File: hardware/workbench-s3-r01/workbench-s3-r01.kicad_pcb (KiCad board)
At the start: 2 copper layers, 126 x 135 mm, 52 parts, among them J1 YD P1 / RIGHT SOCKET / 1x22, J2 DISPLAY HARNESS / 3V3, J4 EXPANSION / 3V3 IO, J5 EXTERNAL BOOT / GPIO0 TO GND, J6 EXTERNAL RESET / EN TO GND, J7 YD P2 / LEFT SOCKET / 1x22, SW1 KEY_1 MX HOTSWAP, SW10 KEY_10 MX HOTSWAP, SW11 KEY_11 MX HOTSWAP, SW12 KEY_12 MX HOTSWAP, SW13 KEY_13 MX HOTSWAP, SW14 KEY_14 MX HOTSWAP, SW15 KEY_15 MX HOTSWAP, SW16 KEY_16 MX HOTSWAP, SW17 KEY_17 MX HOTSWAP, SW18 KEY_18 MX HOTSWAP, SW2 KEY_2 MX HOTSWAP, SW3 KEY_3 MX HOTSWAP, SW4 KEY_4 MX HOTSWAP, SW5 KEY_5 MX HOTSWAP, SW6 KEY_6 MX HOTSWAP, SW7 KEY_7 MX HOTSWAP, SW8 KEY_8 MX HOTSWAP, SW9 KEY_9 MX HOTSWAP

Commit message: Update application workflows and supporting components
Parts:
- removed H1, H2, H3, H4, H5: M3 head <=5.6mm, MountingHole_M3_5.6mm_Head
- added H_L1: M3 head <=5.6mm, MountingHole_M3_5.6mm_Head, F.Cu at (172.0, 233.0)
- added H_L2: M3 head <=5.6mm, MountingHole_M3_5.6mm_Head, F.Cu at (54.0, 233.0)
- added H_L3: M3 head <=5.6mm, MountingHole_M3_5.6mm_Head, F.Cu at (172.0, 155.0)
- added H_L4: M3 head <=5.6mm, MountingHole_M3_5.6mm_Head, F.Cu at (54.0, 155.0)
- added H_U1: M3 head <=5.6mm, MountingHole_M3_5.6mm_Head, F.Cu at (54.0, 54.0)
- added H_U2: M3 head <=5.6mm, MountingHole_M3_5.6mm_Head, F.Cu at (172.0, 54.0)
- added H_U3: M3 head <=5.6mm, MountingHole_M3_5.6mm_Head, F.Cu at (54.0, 144.0)
- added H_U4: M3 head <=5.6mm, MountingHole_M3_5.6mm_Head, F.Cu at (172.0, 144.0)
- added J8: LOWER / IDC20 TO J9 / 1:1, IDC-Header_2x10_P2.54mm_Vertical, F.Cu at (129.0, 212.0)
- added J9: UPPER / IDC20 TO J8 / 1:1, IDC-Header_2x10_P2.54mm_Vertical, B.Cu at (162.0, 65.0)
- added MB1: MouseBites_6x0.5_P0.8, MouseBites_6x0.5_P0.8, F.Cu at (70.0, 148.8)
- added MB2: MouseBites_6x0.5_P0.8, MouseBites_6x0.5_P0.8, F.Cu at (70.0, 150.2)
- added MB3: MouseBites_6x0.5_P0.8, MouseBites_6x0.5_P0.8, F.Cu at (113.0, 148.8)
- added MB4: MouseBites_6x0.5_P0.8, MouseBites_6x0.5_P0.8, F.Cu at (113.0, 150.2)
- added MB5: MouseBites_6x0.5_P0.8, MouseBites_6x0.5_P0.8, F.Cu at (156.0, 148.8)
- added MB6: MouseBites_6x0.5_P0.8, MouseBites_6x0.5_P0.8, F.Cu at (156.0, 150.2)
- moved J4 209.8 mm to (166.0, 234.0), turned to -90 degrees
- moved J6 180.3 mm to (102.0, 233.0), turned to -90 degrees
- moved J5 179.0 mm to (111.0, 233.0), turned to -90 degrees
- moved R3 164.0 mm to (104.0, 225.0), turned to 180 degrees
- moved J1 123.9 mm to (64.3, 181.8), turned to 0 degrees
- moved J7 89.6 mm to (89.7, 181.8), turned to 0 degrees
- moved D10 38.4 mm to (124.0, 111.0)
- moved D11 38.4 mm to (143.1, 111.0)
- moved D12 38.4 mm to (162.1, 111.0)
- moved D7 38.4 mm to (66.9, 111.0)
- moved D8 38.4 mm to (85.9, 111.0)
- moved D9 38.4 mm to (105.0, 111.0)
- moved SW10 38.4 mm to (124.0, 117.0)
- moved SW11 38.4 mm to (143.1, 117.0)
- moved SW12 38.4 mm to (162.1, 117.0)
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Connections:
- net /KEY_10_A renamed /UP_KEY_10_A
- net /KEY_11_A renamed /UP_KEY_11_A
- net /KEY_12_A renamed /UP_KEY_12_A
- net /KEY_13_A renamed /UP_KEY_13_A
- net /KEY_14_A renamed /UP_KEY_14_A
- net /KEY_15_A renamed /UP_KEY_15_A
- net /KEY_16_A renamed /UP_KEY_16_A
- net /KEY_17_A renamed /UP_KEY_17_A
- net /KEY_18_A renamed /UP_KEY_18_A
- net /KEY_1_A renamed /UP_KEY_1_A
- net /KEY_2_A renamed /UP_KEY_2_A
- net /KEY_3_A renamed /UP_KEY_3_A
- net /KEY_4_A renamed /UP_KEY_4_A
- net /KEY_5_A renamed /UP_KEY_5_A
- net /KEY_6_A renamed /UP_KEY_6_A
- net /KEY_7_A renamed /UP_KEY_7_A
- net /KEY_8_A renamed /UP_KEY_8_A
- net /KEY_9_A renamed /UP_KEY_9_A
- C1 pad 1: /+3V3 -> /UP_3V3
- C1 pad 2: /GND -> /UP_GND
- C2 pad 1: /+3V3 -> /UP_3V3
- C2 pad 2: /GND -> /UP_GND
- D1 pad 1: /GPIO4 -> /UP_GPIO4
- D10 pad 1: /GPIO5 -> /UP_GPIO5
- D11 pad 1: /GPIO5 -> /UP_GPIO5
- D12 pad 1: /GPIO5 -> /UP_GPIO5
- D13 pad 1: /GPIO6 -> /UP_GPIO6
- D14 pad 1: /GPIO6 -> /UP_GPIO6
- D15 pad 1: /GPIO6 -> /UP_GPIO6
- D16 pad 1: /GPIO6 -> /UP_GPIO6
- D17 pad 1: /GPIO6 -> /UP_GPIO6
- D18 pad 1: /GPIO6 -> /UP_GPIO6
- D2 pad 1: /GPIO4 -> /UP_GPIO4
- D3 pad 1: /GPIO4 -> /UP_GPIO4
- D4 pad 1: /GPIO4 -> /UP_GPIO4
- D5 pad 1: /GPIO4 -> /UP_GPIO4
- D6 pad 1: /GPIO4 -> /UP_GPIO4
- D7 pad 1: /GPIO5 -> /UP_GPIO5
- D8 pad 1: /GPIO5 -> /UP_GPIO5
- D9 pad 1: /GPIO5 -> /UP_GPIO5
- J2 pad 1: /GND -> /UP_GND
- J2 pad 2: /+3V3 -> /UP_3V3
- J2 pad 3: /GPIO14 -> /UP_GPIO14
- J2 pad 4: /GPIO13 -> /UP_GPIO13
- J2 pad 5: /GPIO15 -> /UP_GPIO15
- J2 pad 6: /GPIO16 -> /UP_GPIO16
- J2 pad 7: /GPIO17 -> /UP_GPIO17
- J2 pad 8: /GPIO18 -> /UP_GPIO18
- J2 pad 9: /GPIO21 -> /UP_GPIO21
- R1 pad 1: /+3V3 -> /UP_3V3
- R1 pad 2: /GPIO13 -> /UP_GPIO13
- R2 pad 1: /+3V3 -> /UP_3V3
- R2 pad 2: /GPIO14 -> /UP_GPIO14
- SW1 pad 1: /GPIO7 -> /UP_GPIO7
- SW10 pad 1: /GPIO10 -> /UP_GPIO10
- SW11 pad 1: /GPIO11 -> /UP_GPIO11
- SW12 pad 1: /GPIO12 -> /UP_GPIO12
- SW13 pad 1: /GPIO7 -> /UP_GPIO7
- SW14 pad 1: /GPIO8 -> /UP_GPIO8
- SW15 pad 1: /GPIO9 -> /UP_GPIO9
- SW16 pad 1: /GPIO10 -> /UP_GPIO10
- SW17 pad 1: /GPIO11 -> /UP_GPIO11
- SW18 pad 1: /GPIO12 -> /UP_GPIO12
- SW2 pad 1: /GPIO8 -> /UP_GPIO8
- SW3 pad 1: /GPIO9 -> /UP_GPIO9
- SW4 pad 1: /GPIO10 -> /UP_GPIO10
- SW5 pad 1: /GPIO11 -> /UP_GPIO11
- SW6 pad 1: /GPIO12 -> /UP_GPIO12
- SW7 pad 1: /GPIO7 -> /UP_GPIO7
- SW8 pad 1: /GPIO8 -> /UP_GPIO8
- SW9 pad 1: /GPIO9 -> /UP_GPIO9
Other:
- board size 126 x 135 mm -> 126 x 187 mm
- board text added: "C1"
- board text added: "C2"
- board text added: "HORIZONTAL / UNROUTED"
- board text added: "J2 DISPLAY / 3V3"
- board text added: "J8 IDC20 / TO UPPER J9"
- board text added: "J9 IDC20 / TO LOWER J8"
- board text added: "LOWER / YD ESP32-S3"
- board text added: "PANEL / 1.6 mm / 2 Cu / NOT FOR FABRICATION"
- board text added: "R1"
- board text added: "R1/R2 DNP"
- board text added: "R2"
- board text added: "R3"
- board text added: "S3 r01 / UNROUTED"
- board text added: "SH1106 + EC11 / PANEL MOUNT"
- board text added: "TRIM TAB STUBS BEFORE ASSEMBLY"
- board text added: "UPPER / 3x6 MATRIX"
- board text removed: "126 x 135 mm / 1.6 mm / 2 Cu layers (proposed)"
- board text removed: "J2 HARNESS: SEE README"
- board text removed: "KIVO WORKBENCH"
- board text removed: "NO ROUTING. NO GERBERS. ENCLOSURE REDESIGN REQUIRED."
- board text removed: "PANEL MOUNT / VERIFY HEIGHT"
- board text removed: "S3 r01 MATRIX / UNROUTED"
- board text removed: "SH1106 + EC11 MODULE"
- board text removed: "YD ESP32-S3"

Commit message: fix: correct Workbench S3 display connector and mounting geometry
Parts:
- added H_D1: M3 head <=5.6mm, MountingHole_M3_5.6mm_Head, F.Cu at (60.9, 55.9)
- added H_D2: M3 head <=5.6mm, MountingHole_M3_5.6mm_Head, F.Cu at (119.9, 55.9)
- added H_D3: M3 head <=5.6mm, MountingHole_M3_5.6mm_Head, F.Cu at (61.0, 85.1)
- added H_D4: M3 head <=5.6mm, MountingHole_M3_5.6mm_Head, F.Cu at (119.9, 84.9)
- J2: value DISPLAY HARNESS / 3V3 -> DISPLAY / MODULE PIN 1 = 3V3
- moved J2 33.3 mm to (89.7, 54.9), turned to -90 degrees
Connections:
- J2 pad 1: /UP_GND -> /UP_3V3
- J2 pad 2: /UP_3V3 -> /UP_GND
- J2 pad 3: /UP_GPIO14 -> /UP_GPIO21
- J2 pad 4: /UP_GPIO13 -> /UP_GPIO18
- J2 pad 5: /UP_GPIO15 -> /UP_GPIO17
- J2 pad 7: /UP_GPIO17 -> /UP_GPIO14
- J2 pad 8: /UP_GPIO18 -> /UP_GPIO13
- J2 pad 9: /UP_GPIO21 -> /UP_GPIO15
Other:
- board text added: "64.90 x 35.03 / 4 x M3"
- board text added: "BAK"
- board text added: "CON"
- board text added: "J2"
- board text added: "PSH"
- board text added: "SH1106 + EC11 / FRONT VIEW"
- board text added: "TRA"
- board text added: "TRB"
- board text added: "VCC"
- board text removed: "A"
- board text removed: "B"
- board text removed: "BACK"
- board text removed: "J2 DISPLAY / 3V3"
- board text removed: "OK"
- board text removed: "PRESS"
- board text removed: "SH1106 + EC11 / PANEL MOUNT"

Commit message: Update application implementation and supporting files
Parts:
- added C3: 100n 16V X7R / U1, C_0805_2012Metric_Pad1.18x1.45mm_HandSolder, F.Cu at (139.0, 74.0)
- added R4: 10k U1 RESET PULLUP, R_0805_2012Metric_Pad1.20x1.40mm_HandSolder, F.Cu at (161.0, 78.0)
- added U1: MCP23017-E/SO / 0x20, SOIC-28W_7.5x17.9mm_P1.27mm, F.Cu at (149.0, 72.0)
- J4: value EXPANSION / 3V3 IO -> EXPANSION / 22 SPARE GPIO / 3V3 IO; footprint PinHeader_1x10_P2.54mm_Vertical -> PinHeader_1x24_P2.54mm_Vertical
- J8: value LOWER / IDC20 TO J9 / 1:1 -> LOWER / I2C4 TO J9 / 1:1; footprint IDC-Header_2x10_P2.54mm_Vertical -> JST_XH_B4B-XH-A_1x04_P2.50mm_Vertical
- J9: value UPPER / IDC20 TO J8 / 1:1 -> UPPER / I2C4 TO J8 / 1:1; footprint IDC-Header_2x10_P2.54mm_Vertical -> JST_XH_B4B-XH-A_1x04_P2.50mm_Vertical
- R1, R2: value 4.7k DNP -> 2.2k I2C PULLUP
- moved J9 29.8 mm to (133.0, 58.0), turned to 0 degrees
- moved R1 23.0 mm to (128.0, 78.0)
- moved R2 23.0 mm to (133.0, 78.0)
- moved C1 14.4 mm to (127.0, 70.0)
- moved C2 14.4 mm to (132.0, 70.0)
- moved J5 8.00 mm to (103.0, 233.0)
- moved J6 6.00 mm to (96.0, 233.0)
- turned J8 to 180 degrees
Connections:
- D1 pad 1: /UP_GPIO4 -> /UP_GPA5
- D10 pad 1: /UP_GPIO5 -> /UP_GPA6
- D11 pad 1: /UP_GPIO5 -> /UP_GPA6
- D12 pad 1: /UP_GPIO5 -> /UP_GPA6
- D13 pad 1: /UP_GPIO6 -> /UP_GPA7
- D14 pad 1: /UP_GPIO6 -> /UP_GPA7
- D15 pad 1: /UP_GPIO6 -> /UP_GPA7
- D16 pad 1: /UP_GPIO6 -> /UP_GPA7
- D17 pad 1: /UP_GPIO6 -> /UP_GPA7
- D18 pad 1: /UP_GPIO6 -> /UP_GPA7
- D2 pad 1: /UP_GPIO4 -> /UP_GPA5
- D3 pad 1: /UP_GPIO4 -> /UP_GPA5
- D4 pad 1: /UP_GPIO4 -> /UP_GPA5
- D5 pad 1: /UP_GPIO4 -> /UP_GPA5
- D6 pad 1: /UP_GPIO4 -> /UP_GPA5
- D7 pad 1: /UP_GPIO5 -> /UP_GPA6
- D8 pad 1: /UP_GPIO5 -> /UP_GPA6
- D9 pad 1: /UP_GPIO5 -> /UP_GPA6
- J2 pad 3: /UP_GPIO21 -> /UP_GPA4
- J2 pad 4: /UP_GPIO18 -> /UP_GPA3
- J2 pad 5: /UP_GPIO17 -> /UP_GPA2
- J2 pad 6: /UP_GPIO16 -> /UP_GPA1
- J2 pad 9: /UP_GPIO15 -> /UP_GPA0
- J4 pad 10: /GPIO47 -> /GPIO9
- J4 pad 5: /GPIO38 -> /GPIO4
- J4 pad 6: /GPIO39 -> /GPIO5
- J4 pad 7: /GPIO40 -> /GPIO6
- J4 pad 8: /GPIO41 -> /GPIO7
- J4 pad 9: /GPIO42 -> /GPIO8
- J8 pad 3: /GPIO4 -> /GPIO13
- J8 pad 4: /GPIO5 -> /GPIO14
- J9 pad 3: /UP_GPIO4 -> /UP_GPIO13
- J9 pad 4: /UP_GPIO5 -> /UP_GPIO14
- SW1 pad 1: /UP_GPIO7 -> /UP_GPB0
- SW10 pad 1: /UP_GPIO10 -> /UP_GPB3
- SW11 pad 1: /UP_GPIO11 -> /UP_GPB4
- SW12 pad 1: /UP_GPIO12 -> /UP_GPB5
- SW13 pad 1: /UP_GPIO7 -> /UP_GPB0
- SW14 pad 1: /UP_GPIO8 -> /UP_GPB1
- SW15 pad 1: /UP_GPIO9 -> /UP_GPB2
- SW16 pad 1: /UP_GPIO10 -> /UP_GPB3
- SW17 pad 1: /UP_GPIO11 -> /UP_GPB4
- SW18 pad 1: /UP_GPIO12 -> /UP_GPB5
- SW2 pad 1: /UP_GPIO8 -> /UP_GPB1
- SW3 pad 1: /UP_GPIO9 -> /UP_GPB2
- SW4 pad 1: /UP_GPIO10 -> /UP_GPB3
- SW5 pad 1: /UP_GPIO11 -> /UP_GPB4
- SW6 pad 1: /UP_GPIO12 -> /UP_GPB5
- SW7 pad 1: /UP_GPIO7 -> /UP_GPB0
- SW8 pad 1: /UP_GPIO8 -> /UP_GPB1
- SW9 pad 1: /UP_GPIO9 -> /UP_GPB2
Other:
- board text added: "C3"
- board text added: "GP10"
- board text added: "GP11"
- board text added: "GP12"
- board text added: "GP15"
- board text added: "GP16"
- board text added: "GP17"
- board text added: "GP18"
- board text added: "GP21"
- board text added: "GP4"
- board text added: "GP5"
- board text added: "GP6"
- board text added: "GP7"
- board text added: "GP8"
- board text added: "GP9"
- board text added: "J4 / 22 GPIO / 3V3 IO"
- board text added: "J8 I2C4 / TO UPPER J9"
- board text added: "J9 I2C4 / TO J8"
- board text added: "MCP23017 / 0x20"
- board text added: "R1/R2 2.2k"
- board text added: "R4"
- board text added: "UPPER / I2C4"
- board text removed: "J4 / 3V3 IO"
- board text removed: "J8 IDC20 / TO UPPER J9"
- board text removed: "J9 IDC20 / TO LOWER J8"
- board text removed: "R1/R2 DNP"
- board text removed: "UPPER / 3x6 MATRIX"

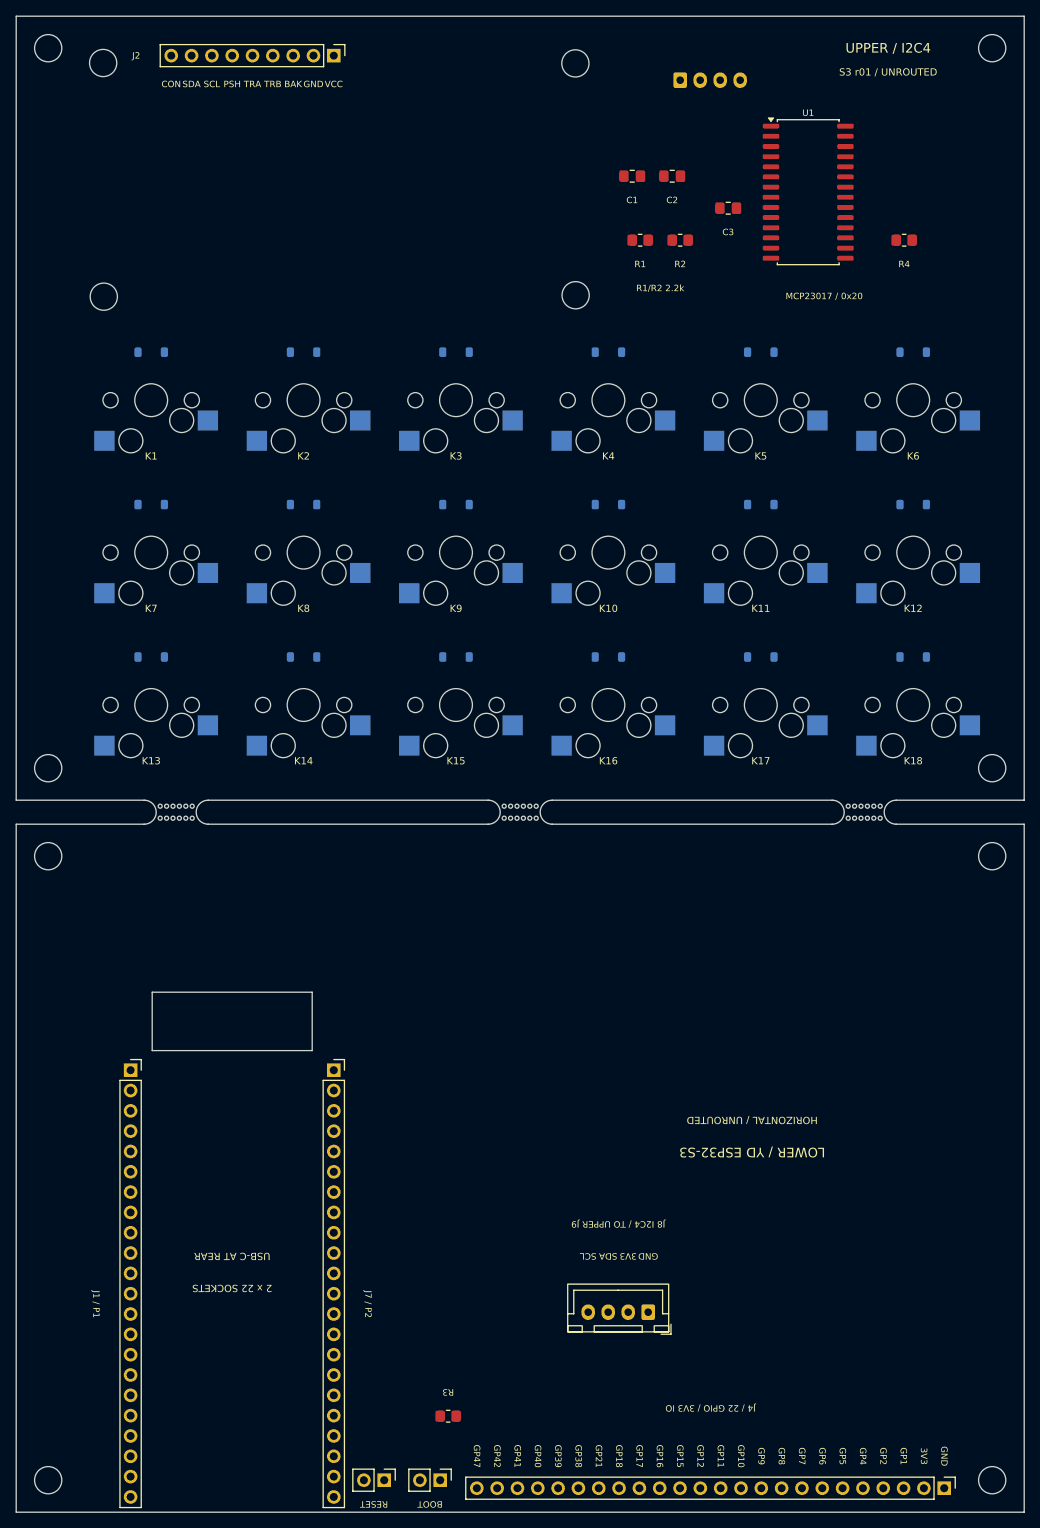
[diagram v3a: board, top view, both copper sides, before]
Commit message: Update device profile layouts and supporting resources
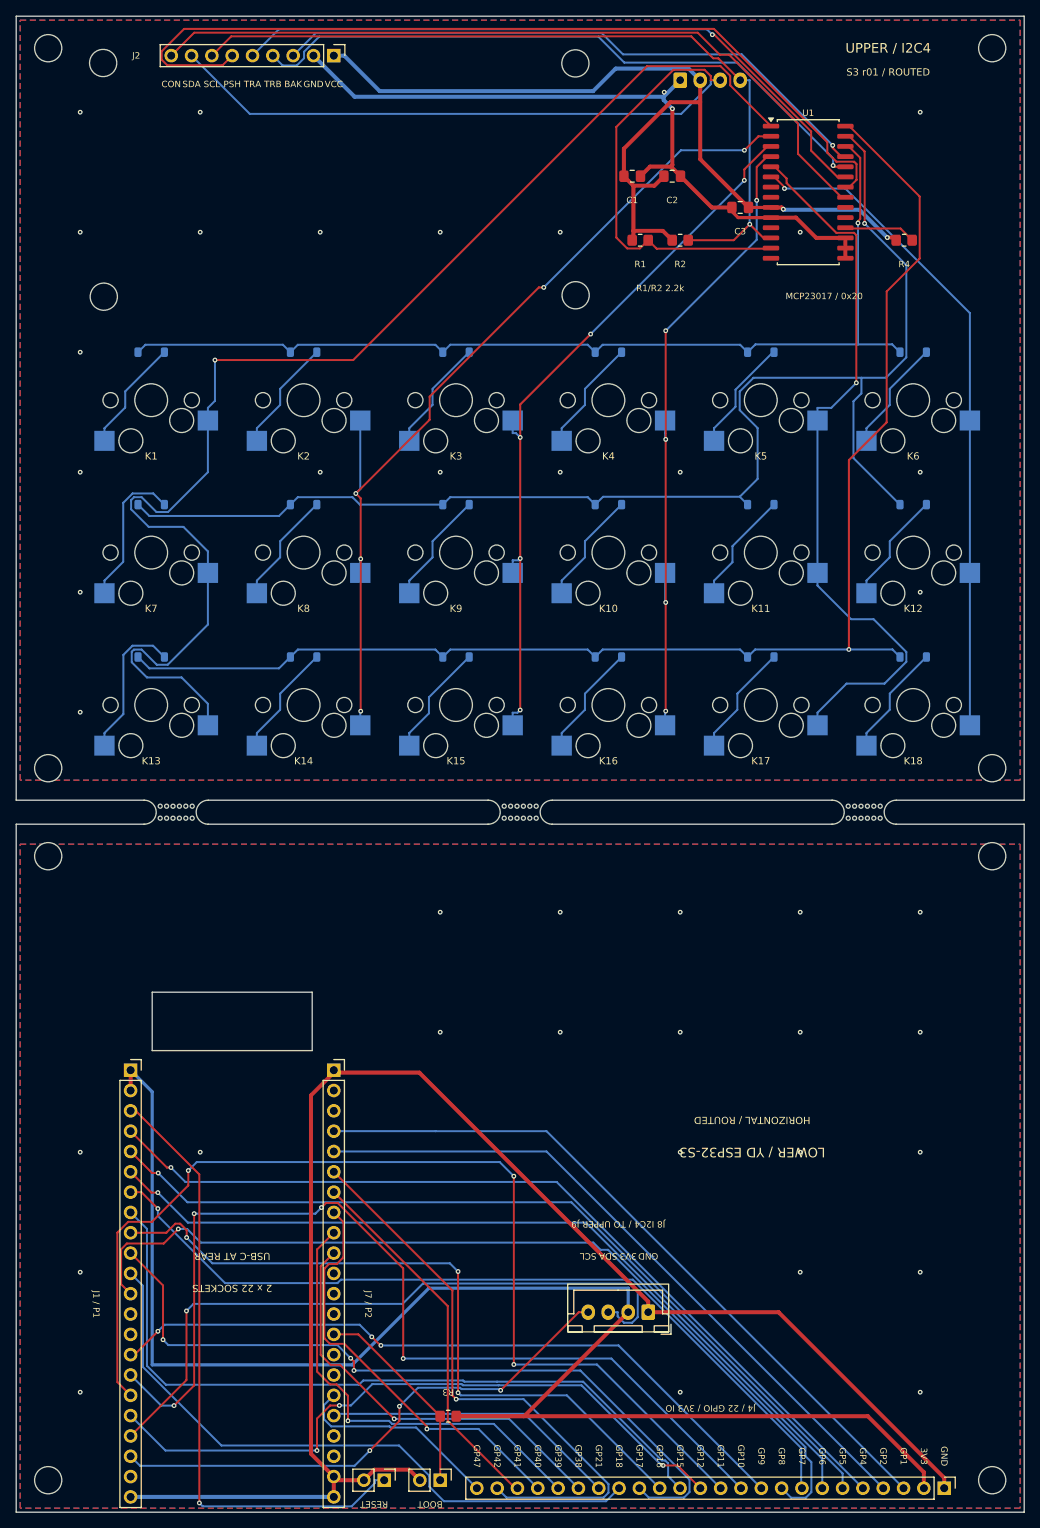
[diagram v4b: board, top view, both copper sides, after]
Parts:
- moved C3 1.50 mm to (140.5, 73.9), turned to 180 degrees
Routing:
- net /+3V3: track 0.00 -> 197.2 mm
- net /GND: track 0.00 -> 192.3 mm, vias 0 -> 21
- net /UP_GPA7: track 0.00 -> 172.7 mm, vias 0 -> 1
- net /UP_GPA6: track 0.00 -> 167.1 mm, vias 0 -> 1
- net /UP_GPB0: track 0.00 -> 165.7 mm, vias 0 -> 1
- net /GPIO11: track 0.00 -> 131.8 mm, vias 0 -> 3
- net /UP_GPA5: track 0.00 -> 125.0 mm, vias 0 -> 1
- net /UP_GPIO13: track 0.00 -> 122.6 mm
- net /GPIO10: track 0.00 -> 122.3 mm, vias 0 -> 4
- net /UP_3V3: track 0.00 -> 121.5 mm, vias 0 -> 2
- net /GPIO8: track 0.00 -> 114.4 mm, vias 0 -> 1
- net /UP_GPB1: track 0.00 -> 112.5 mm, vias 0 -> 5
- net /UP_GPA1: track 0.00 -> 110.2 mm
- net /GPIO4: track 0.00 -> 110.0 mm, vias 0 -> 1
- net /GPIO5: track 0.00 -> 107.5 mm, vias 0 -> 1
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- added copper zone on B.Cu, net /GND
- added copper zone on F.Cu, net /GND
- added copper zone on B.Cu, net /UP_GND
- added copper zone on F.Cu, net /UP_GND
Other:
- board text added: "HORIZONTAL / ROUTED"
- board text added: "PANEL / 1.6 mm / 2 Cu / FIT CHECK PENDING"
- board text added: "S3 r01 / ROUTED"
- board text removed: "HORIZONTAL / UNROUTED"
- board text removed: "PANEL / 1.6 mm / 2 Cu / NOT FOR FABRICATION"
- board text removed: "S3 r01 / UNROUTED"
